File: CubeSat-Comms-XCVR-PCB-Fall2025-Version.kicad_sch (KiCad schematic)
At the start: 68 parts, among them J1 Screw_Terminal_01x02, J2 Screw_Terminal_01x02, J3 Conn_Coaxial, J4 Conn_01x12_Pin, U1 CC1101RGP, U2 SKY65366-21, U3 PE4251MLI-Z, U4 NCP186AMX390TAG, Y1 NX3225GA-26MHZ-TI

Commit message: updated mounting holes to have plated connections
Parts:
- H1, H2, H3, H4: footprint MountingHole:MountingHole_2.2mm_M2 -> MountingHole:MountingHole_2.2mm_M2_DIN965_Pad_TopBottom
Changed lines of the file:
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@@
 			)
 		)
-		(property "Footprint" "MountingHole:MountingHole_2.2mm_M2"
+		(property "Footprint" "MountingHole:MountingHole_2.2mm_M2_DIN965_Pad_TopBottom"
 			(at 321.31 226.06 0)
 			(effects
@@
 			)
 		)
-		(property "Footprint" "MountingHole:MountingHole_2.2mm_M2"
+		(property "Footprint" "MountingHole:MountingHole_2.2mm_M2_DIN965_Pad_TopBottom"
 			(at 321.31 219.71 0)
 			(effects
@@
 			)
 		)
-		(property "Footprint" "MountingHole:MountingHole_2.2mm_M2"
+		(property "Footprint" "MountingHole:MountingHole_2.2mm_M2_DIN965_Pad_TopBottom"
 			(at 321.31 238.76 0)
 			(effects
@@
 			)
 		)
-		(property "Footprint" "MountingHole:MountingHole_2.2mm_M2"
+		(property "Footprint" "MountingHole:MountingHole_2.2mm_M2_DIN965_Pad_TopBottom"
 			(at 321.31 232.41 0)
 			(effects

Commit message: updated trace wiring
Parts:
- H1, H2, H3, H4: footprint MountingHole:MountingHole_2.2mm_M2_DIN965_Pad_TopBottom -> MountingHole:MountingHole_3.2mm_M3_DIN965_Pad_TopBottom
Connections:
- net BYP: now also J4.11 (Pin_11); no longer J4.9 (Pin_9)
- net EN: now also J4.10 (Pin_10); no longer J4.8 (Pin_8)
- net GD00: now also J4.6 (Pin_6); no longer J4.4 (Pin_4)
- net GD02: now also J4.1 (Pin_1); no longer J4.3 (Pin_3)
- net GND: now also U3.7 (GND)
- net RX0: now also C17.1; no longer C18.1
- net SCLK: now also J4.3 (Pin_3); no longer J4.1 (Pin_1)
- net SI: now also J4.4 (Pin_4); no longer J4.6 (Pin_6)
- net TR: now also J4.9 (Pin_9); no longer J4.7 (Pin_7)
- net TX: now also C18.1; no longer C17.1
- net VPC: now also J4.12 (Pin_12); no longer J4.10 (Pin_10)
- net RF1_STATUS renamed V1
- net V1: now also J4.7 (Pin_7); no longer J4.12 (Pin_12)
- net RF2_STATUS renamed V2
- net V2: now also J4.8 (Pin_8); no longer J4.11 (Pin_11)
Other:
- note added: "Mounting Holes M3"
- note added: "RF1_STATUS (TX)"
- note added: "RF2_STATUS (RX)"
- note removed: "Mounting Holes M2"

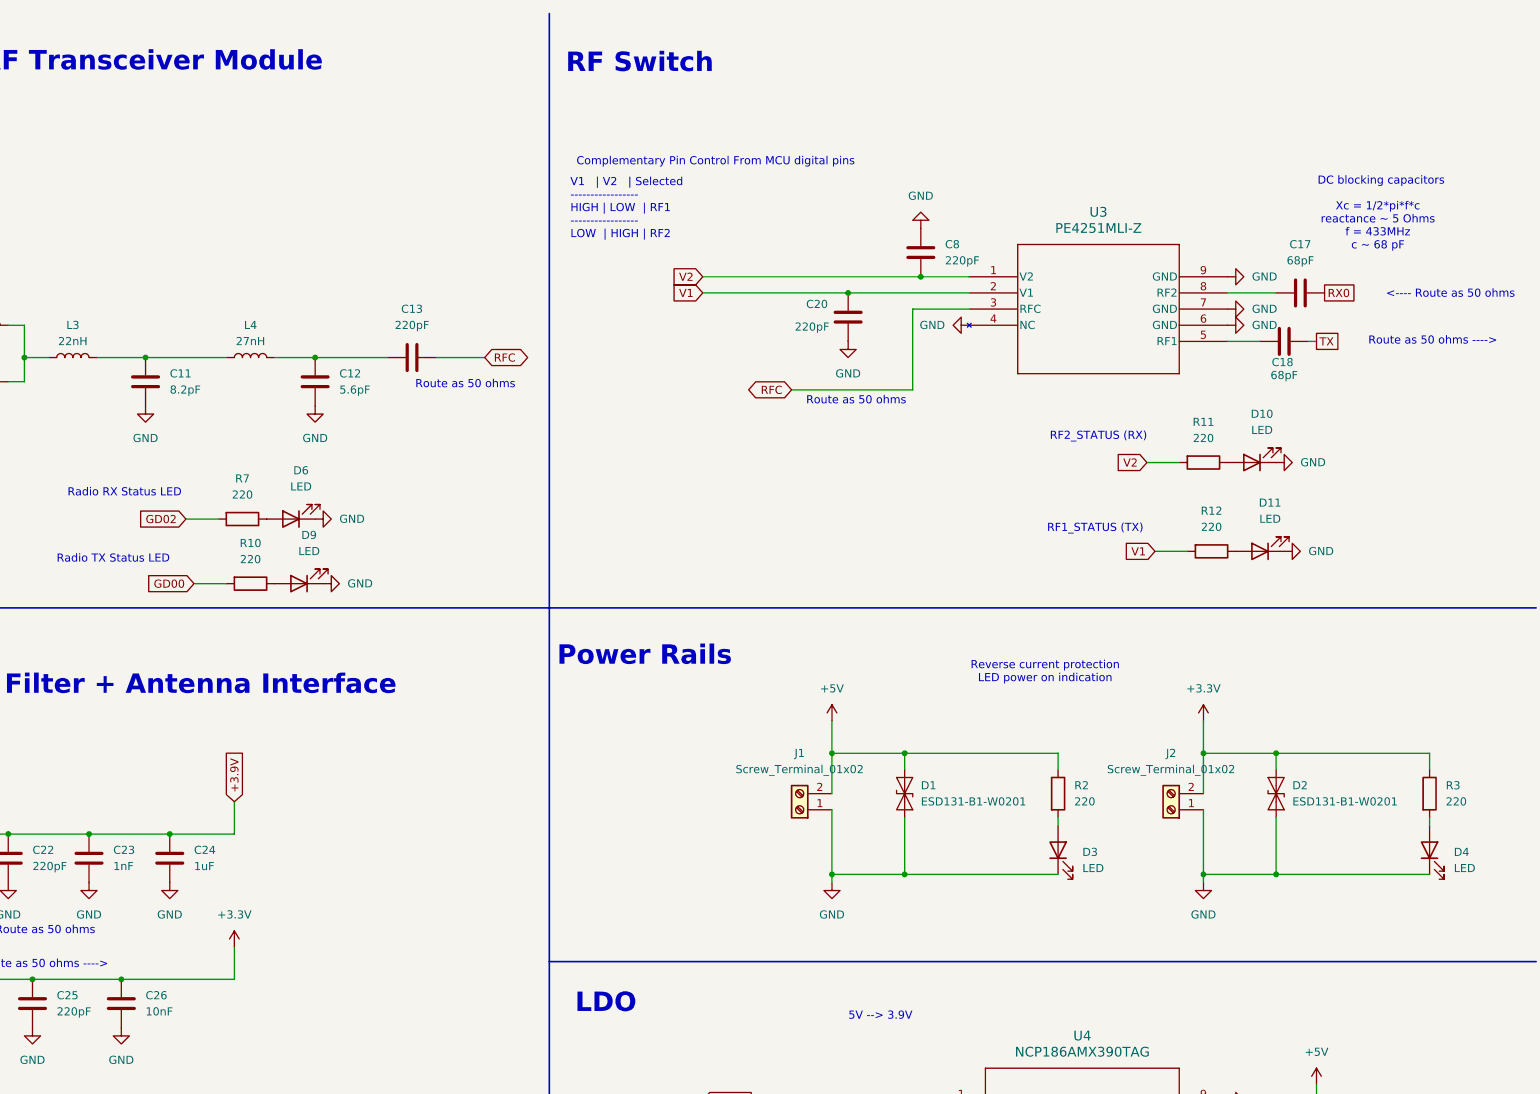
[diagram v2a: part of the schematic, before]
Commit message: revised TVS ESD protection diodes, added JST XH connectors for power
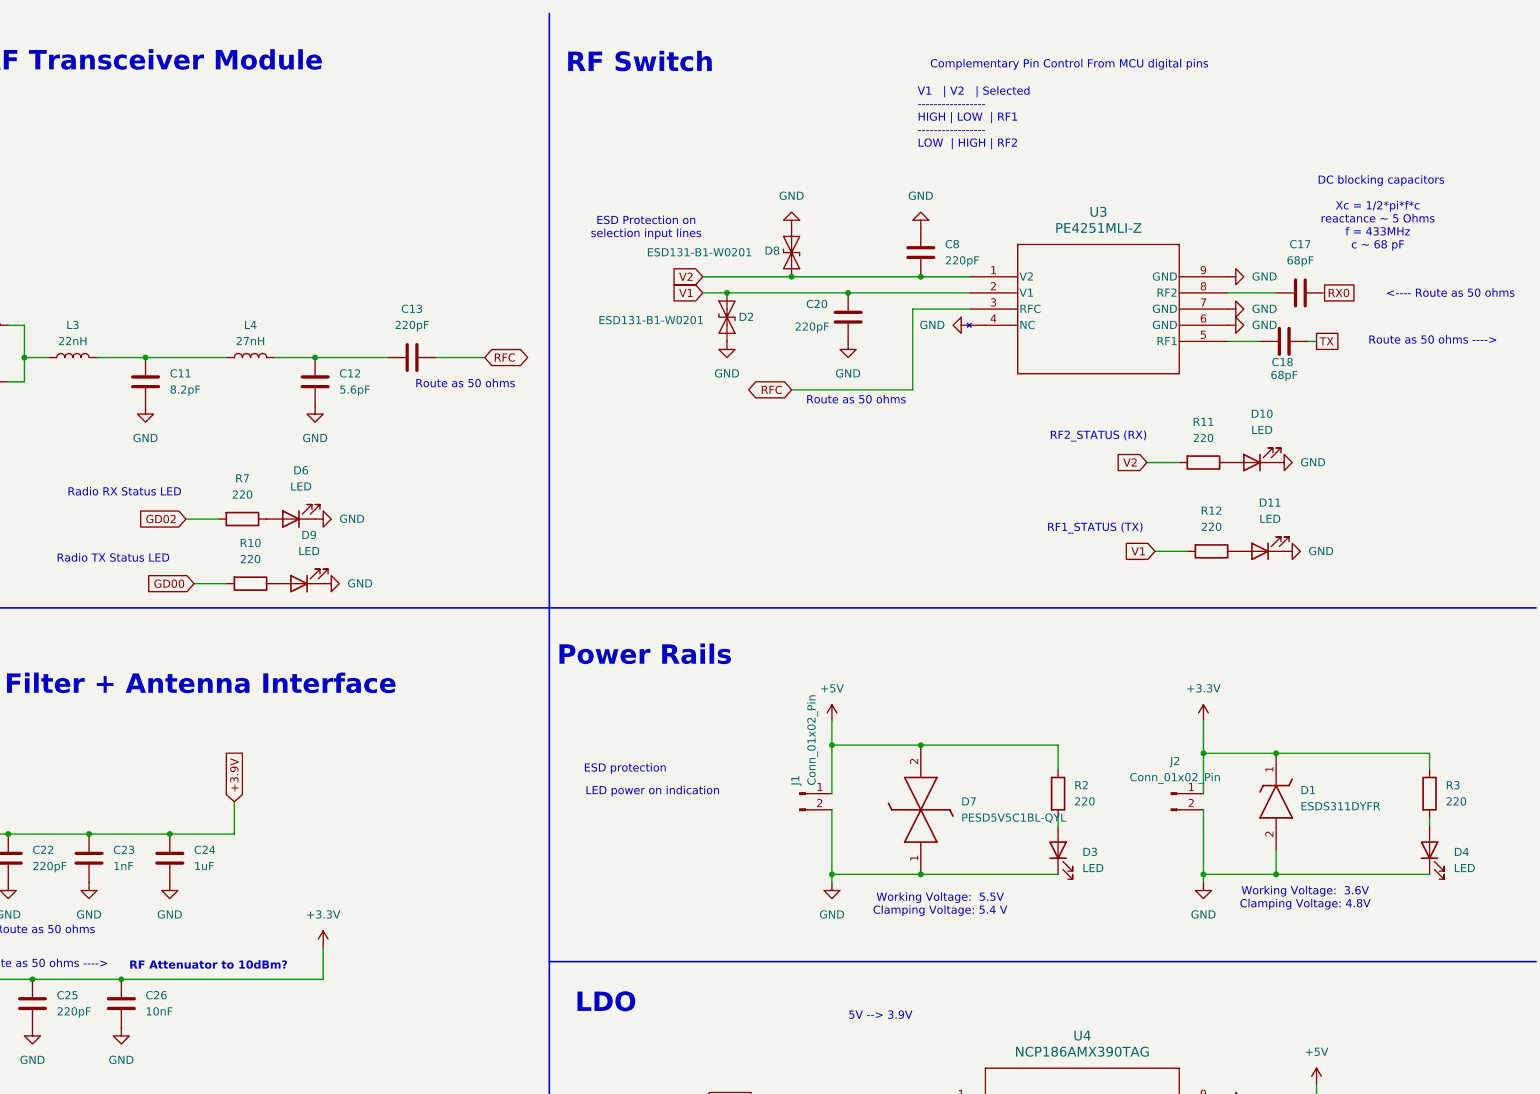
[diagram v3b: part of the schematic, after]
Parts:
- removed D1: ESD131-B1-W0201, Diode_SMD:Infineon_SG-WLL-2-3_0.58x0.28_P0.36mm, symbol Diode:ESD131-B1-W0201
- removed J1, J2: Screw_Terminal_01x02, TerminalBlock_Phoenix:TerminalBlock_Phoenix_MKDS-1,5-2-5.08_1x02_P5.08mm_Horizontal, symbol Connector:Screw_Terminal_01x02
- added D1: ESDS311DYFR, ESDS311DYFR, symbol comms-board-symbols:ESDS311DYFR
- added D7: PESD5V5C1BL-QYL, PESD5V5C1BLQYL, symbol comms-board-symbols:PESD5V5C1BL-QYL
- added D8: ESD131-B1-W0201, Diode_SMD:Infineon_SG-WLL-2-3_0.58x0.28_P0.36mm, symbol Diode:ESD131-B1-W0201
- added J1, J2: Conn_01x02_Pin, Connector_JST:JST_XH_B2B-XH-A_1x02_P2.50mm_Vertical, symbol Connector:Conn_01x02_Pin
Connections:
- net +3.3V: now also D1.1 (K), J2.1 (Pin_1); no longer D2.2 (A2)
- net +5V: now also D7.2 (K2), J1.1 (Pin_1)
- net GND: now also D1.2 (A), D7.1 (K1), D8.1 (A1), J1.2 (Pin_2), J2.2 (Pin_2)
- net V1: now also D2.2 (A2)
- net V2: now also D8.2 (A2)
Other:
- note added: "ESD Protection on selection input lines"
- note added: "ESD protection"
- note added: "LED power on indication"
- note added: "RF Attenuator to 10dBm?"
- note added: "Working Voltage: 3.6V Clamping Voltage: 4.8V"
- note added: "Working Voltage: 5.5V Clamping Voltage: 5.4 V"
- note removed: "Reverse current protection LED power on indication"
- moved on the sheet: D2

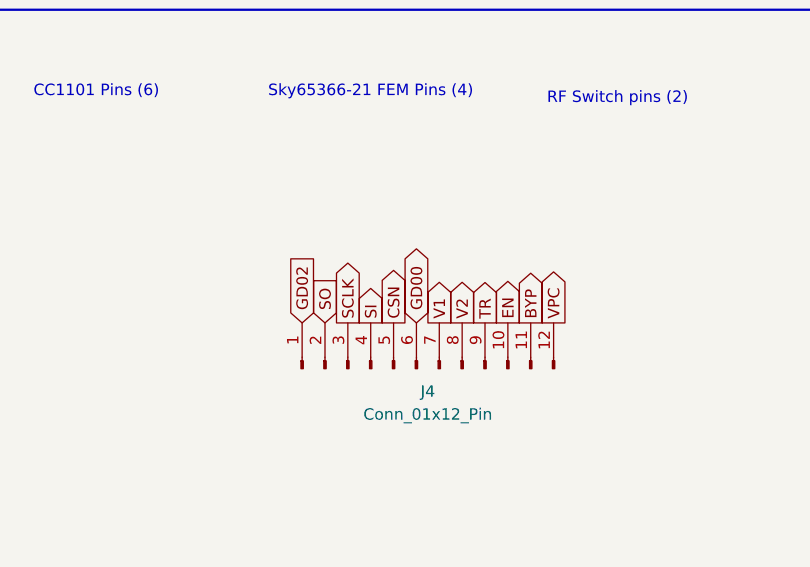
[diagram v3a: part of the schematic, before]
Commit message: pcb edits: sticking vias, trace routing...
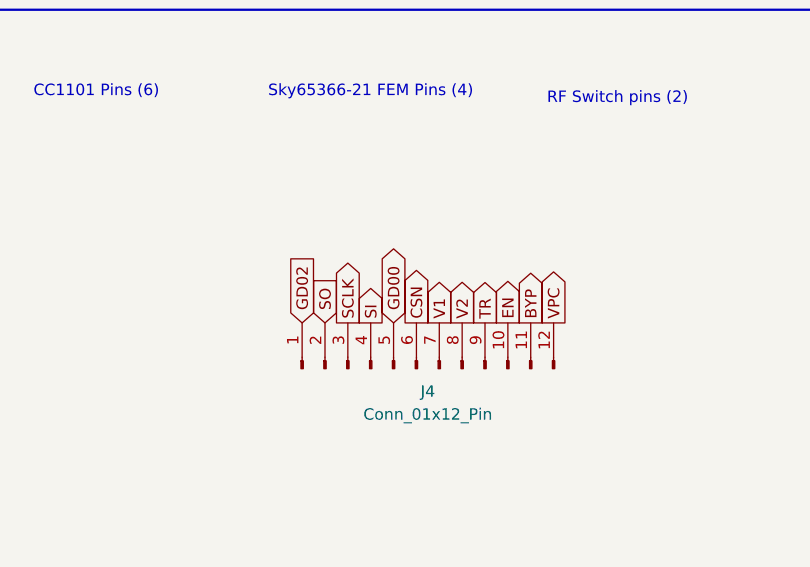
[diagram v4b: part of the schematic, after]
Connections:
- net CSN: now also J4.6 (Pin_6); no longer J4.5 (Pin_5)
- net GD00: now also J4.5 (Pin_5); no longer J4.6 (Pin_6)
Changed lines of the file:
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@@
 	(global_label "GD00"
 		(shape bidirectional)
-		(at 66.04 245.11 90)
-		(fields_autoplaced yes)
-		(effects
-			(font
-				(size 1.27 1.27)
-			)
-			(justify left)
-		)
-		(property "Intersheetrefs" "${INTERSHEET_REFS}"
-			(at 66.04 236.0545 90)
+		(at 63.5 245.11 90)
+		(fields_autoplaced yes)
+		(effects
+			(font
+				(size 1.27 1.27)
+			)
+			(justify left)
+		)
+		(property "Intersheetrefs" "${INTERSHEET_REFS}"
+			(at 63.5 236.0545 90)
 			(effects
 				(font
@@
 	(global_label "CSN"
 		(shape output)
-		(at 63.5 245.11 90)
-		(fields_autoplaced yes)
-		(effects
-			(font
-				(size 1.27 1.27)
-			)
-			(justify left)
-		)
-		(property "Intersheetrefs" "${INTERSHEET_REFS}"
-			(at 63.5 238.3148 90)
-			(effects
-				(font
+		(at 66.04 245.11 90)
+		(fields_autoplaced yes)
+		(effects
+			(font
+				(size 1.27 1.27)
+			)
+			(justify left)
+		)
+		(property "Intersheetrefs" "${INTERSHEET_REFS}"
+			(at 66.04 238.3148 90)
+			(effects
+				(font

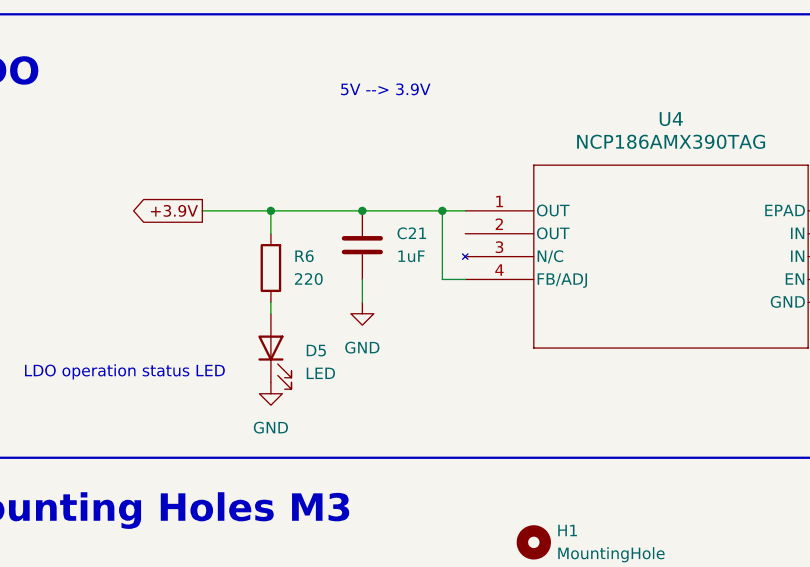
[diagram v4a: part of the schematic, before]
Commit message: revised board clearance rules, drc, routing, placements. TODO = redundant xcvr, impedance matching
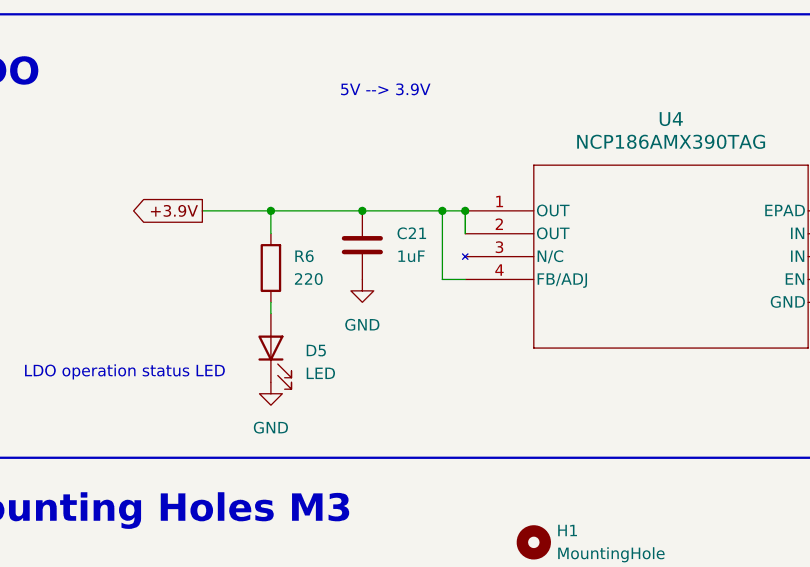
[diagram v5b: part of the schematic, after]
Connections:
- net +3.9V: now also U4.2 (OUT)
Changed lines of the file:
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@@
 	)
 	(junction
+		(at 313.69 182.88)
+		(diameter 0)
+		(color 0 0 0 0)
+	)
+	(junction
 		(at 367.03 147.32)
 		(diameter 0)
@@
 	(wire
 		(pts
+			(xy 313.69 182.88) (xy 313.69 185.42)
+		)
+		(stroke
+			(width 0)
+			(type default)
+		)
+	)
+	(wire
+		(pts
 			(xy 50.8 170.18) (xy 50.8 166.37)
 		)
@@
 	(wire
 		(pts
-			(xy 302.26 190.5) (xy 302.26 193.04)
-		)
-		(stroke
-			(width 0)
-			(type default)
-		)
-	)
-	(wire
-		(pts
 			(xy 124.46 69.85) (xy 124.46 62.23)
 		)
@@
 	(symbol
 		(lib_id "power:GND")
-		(at 302.26 193.04 0)
+		(at 302.26 190.5 0)
 		(unit 1)
 		(exclude_from_sim no)
@@
 		(fields_autoplaced yes)
 		(property "Reference" "#PWR028"
-			(at 302.26 199.39 0)
+			(at 302.26 196.85 0)
 			(effects
 				(font
@@
 		)
 		(property "Value" "GND"
-			(at 302.26 198.12 0)
+			(at 302.26 195.58 0)
 			(effects
 				(font
@@
 		)
 		(property "Footprint" ""
-			(at 302.26 193.04 0)
+			(at 302.26 190.5 0)
 			(effects
 				(font
@@
 		)
 		(property "Datasheet" ""
-			(at 302.26 193.04 0)
+			(at 302.26 190.5 0)
 			(effects
 				(font
@@
 		)
 		(property "Description" "Power symbol creates a global label with name \"GND\" , ground"
-			(at 302.26 193.04 0)
+			(at 302.26 190.5 0)
 			(effects
 				(font

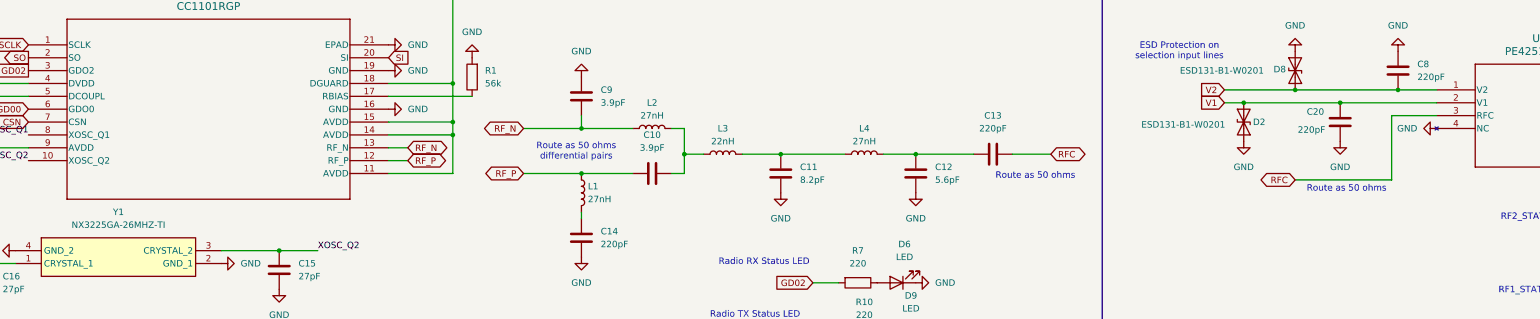
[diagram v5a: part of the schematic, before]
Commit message: editted silk screen and note on schematic about via tenting for CC1101 epad vias
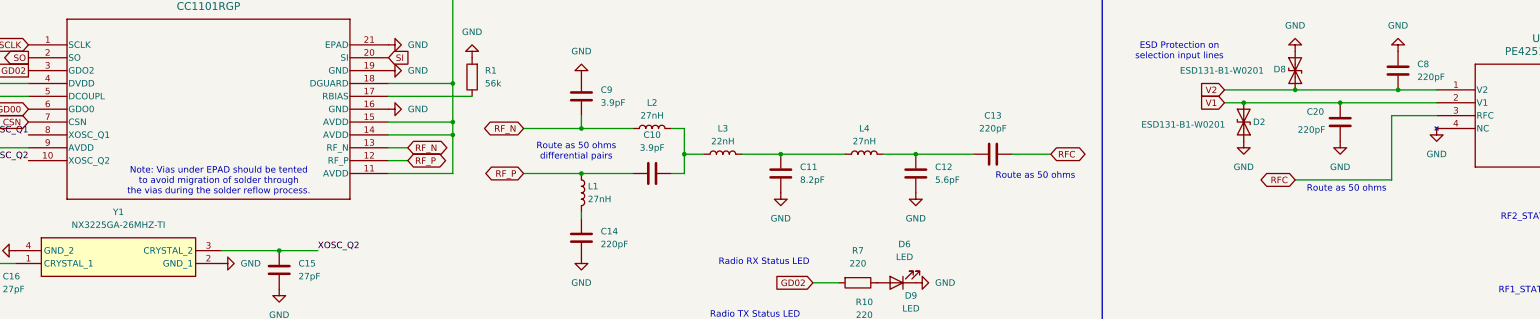
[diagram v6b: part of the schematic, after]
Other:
- note added: "Note: Vias under EPAD should be tented to avoid migration of solder through the vias during the solder reflow process."
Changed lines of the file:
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@@
 		)
 	)
+	(text "Note: Vias under EPAD should be tented \nto avoid migration of solder through \nthe vias during the solder reflow process."
+		(exclude_from_sim no)
+		(at 78.232 71.374 0)
+		(effects
+			(font
+				(size 1.27 1.27)
+			)
+		)
+	)
 	(text "Route as 50 ohms\ndifferential pairs"
 		(exclude_from_sim no)
@@
 	(symbol
 		(lib_id "power:GND")
+		(at 318.77 60.96 0)
+		(unit 1)
+		(exclude_from_sim no)
+		(in_bom yes)
+		(on_board yes)
+		(dnp no)
+		(fields_autoplaced yes)
+		(property "Reference" "#PWR010"
+			(at 318.77 67.31 0)
+			(effects
+				(font
+					(size 1.27 1.27)
+				)
+				(hide yes)
+			)
+		)
+		(property "Value" "GND"
+			(at 318.77 66.04 0)
+			(effects
+				(font
+					(size 1.27 1.27)
+				)
+			)
+		)
+		(property "Footprint" ""
+			(at 318.77 60.96 0)
+			(effects
+				(font
+					(size 1.27 1.27)
+				)
+				(hide yes)
+			)
+		)
+		(property "Datasheet" ""
+			(at 318.77 60.96 0)
+			(effects
+				(font
+					(size 1.27 1.27)
+				)
+				(hide yes)
+			)
+		)
+		(property "Description" "Power symbol creates a global label with name \"GND\" , ground"
+			(at 318.77 60.96 0)
+			(effects
+				(font
+					(size 1.27 1.27)
+				)
+				(hide yes)
+			)
+		)
+		(pin "1"
+		)
+		(instances
+			(project "CubeSat-Comms-XCVR-PCB-Fall2025-Version"
+				(path "/e925e34e-4730-4918-b470-5da5a02639a8"
+					(reference "#PWR010")
+					(unit 1)
+				)
+			)
+		)
+	)
+	(symbol
+		(lib_id "power:GND")
 		(at 153.67 158.75 90)
 		(unit 1)
@@
 	)
 	(symbol
-		(lib_id "power:GND")
-		(at 318.77 60.96 270)
-		(unit 1)
-		(exclude_from_sim no)
-		(in_bom yes)
-		(on_board yes)
-		(dnp no)
-		(fields_autoplaced yes)
-		(property "Reference" "#PWR010"
-			(at 312.42 60.96 0)
-			(effects
-				(font
-					(size 1.27 1.27)
-				)
-				(hide yes)
-			)
-		)
-		(property "Value" "GND"
-			(at 314.96 60.9599 90)
-			(effects
-				(font
-					(size 1.27 1.27)
-				)
-				(justify right)
-			)
-		)
-		(property "Footprint" ""
-			(at 318.77 60.96 0)
-			(effects
-				(font
-					(size 1.27 1.27)
-				)
-				(hide yes)
-			)
-		)
-		(property "Datasheet" ""
-			(at 318.77 60.96 0)
-			(effects
-				(font
-					(size 1.27 1.27)
-				)
-				(hide yes)
-			)
-		)
-		(property "Description" "Power symbol creates a global label with name \"GND\" , ground"
-			(at 318.77 60.96 0)
-			(effects
-				(font
-					(size 1.27 1.27)
-				)
-				(hide yes)
-			)
-		)
-		(pin "1"
-		)
-		(instances
-			(project "CubeSat-Comms-XCVR-PCB-Fall2025-Version"
-				(path "/e925e34e-4730-4918-b470-5da5a02639a8"
-					(reference "#PWR010")
-					(unit 1)
-				)
-			)
-		)
-	)
-	(symbol
 		(lib_id "Device:R")
 		(at 355.6 82.55 270)
@@
 			)
 		)
-		(property "Datasheet" "PE4251MLI-Z"
+		(property "Datasheet" "https://www.psemi.com/pdf/datasheets/pe4251ds.pdf"
 			(at 318.77 53.34 0)
 			(effects
@@
 			(at 318.77 53.34 0)
 			(effects
+				(font
+					(size 1.27 1.27)
+				)
+				(hide yes)
+			)
+		)
+		(property "Field7" ""
+			(at 318.77 53.34 0)
+			(effects
